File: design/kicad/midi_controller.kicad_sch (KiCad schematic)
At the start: 4 parts, among them U1 CD74HC4067M

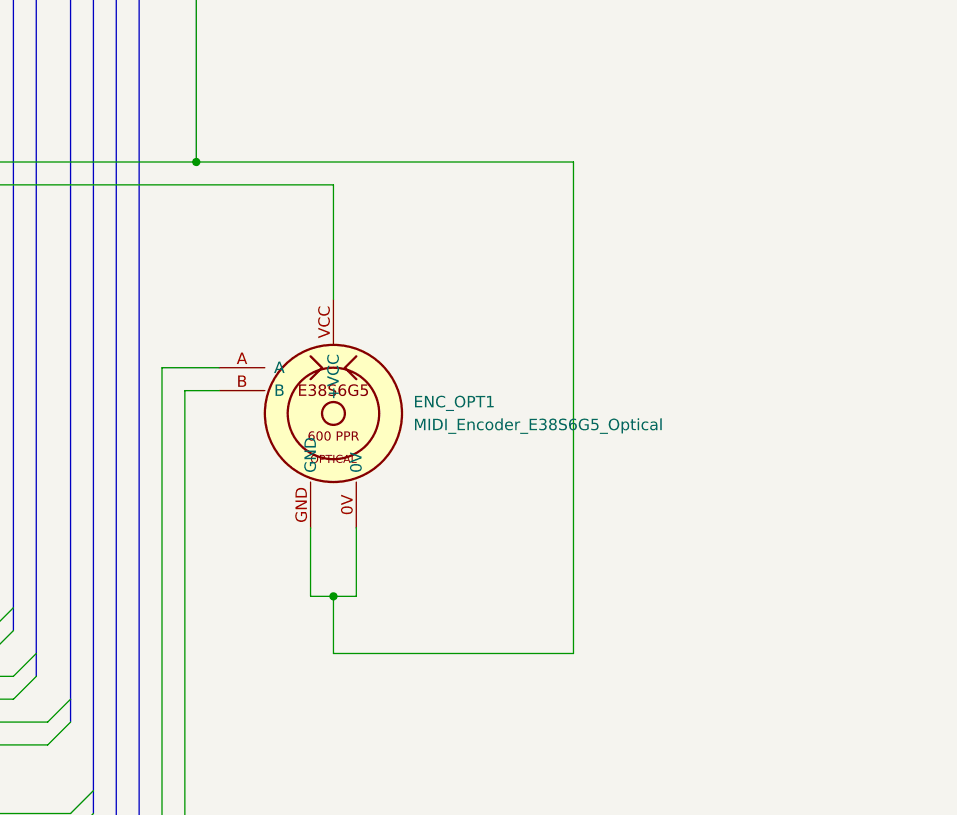
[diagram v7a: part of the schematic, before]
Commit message: Update kicad binary files
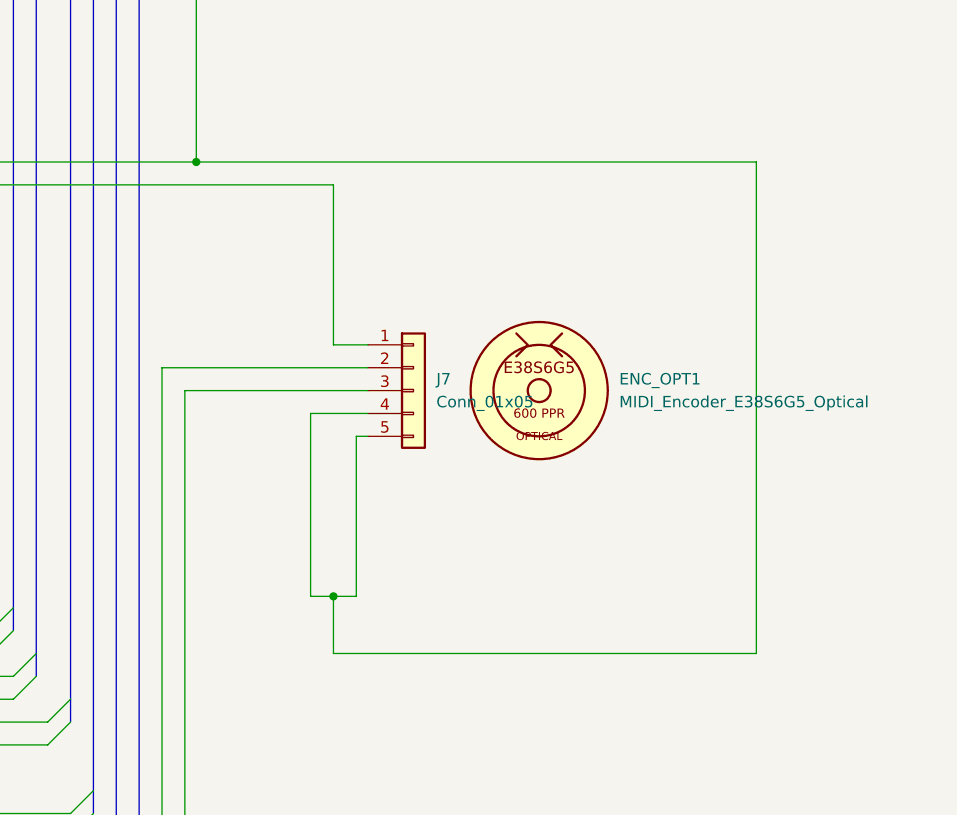
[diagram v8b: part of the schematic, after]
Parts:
- added J7: Conn_01x05, Connector_JST:JST_XH_B5B-XH-A_1x05_P2.50mm_Vertical, symbol Connector_Generic:Conn_01x05
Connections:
- net Buttons_Momentary/GND: now also J7.4 (GND), J7.5 (0V); no longer ENC_OPT1.0V, ENC_OPT1.GND
- net at MCU1.25 (33_MCLK2): now also J7.3 (B); no longer ENC_OPT1.B
- net at MCU1.26 (34_RX8): now also J7.2 (A); no longer ENC_OPT1.A
- net at MCU1.48 (VIN): now also J7.1 (VCC); no longer ENC_OPT1.VCC (+VCC)
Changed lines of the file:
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@@
 	(wire
 		(pts
-			(xy 314.96 146.05) (xy 314.96 158.75)
+			(xy 314.96 146.05) (xy 314.96 163.83)
 		)
 		(stroke
@@
 	(wire
 		(pts
-			(xy 298.45 168.91) (xy 302.26 168.91)
+			(xy 298.45 168.91) (xy 318.77 168.91)
 		)
 		(stroke
@@
 	(wire
 		(pts
+			(xy 312.42 171.45) (xy 312.42 191.77)
+		)
+		(stroke
+			(width 0)
+			(type default)
+		)
+	)
+	(wire
+		(pts
 			(xy 214.63 220.98) (xy 288.29 220.98)
 		)
@@
 	(wire
 		(pts
-			(xy 312.42 184.15) (xy 312.42 191.77)
-		)
-		(stroke
-			(width 0)
-			(type default)
-		)
-	)
-	(wire
-		(pts
 			(xy 125.73 198.12) (xy 158.75 198.12)
 		)
@@
 	(wire
 		(pts
-			(xy 341.63 143.51) (xy 299.72 143.51)
+			(xy 361.95 143.51) (xy 299.72 143.51)
 		)
 		(stroke
@@
 	(wire
 		(pts
+			(xy 312.42 171.45) (xy 318.77 171.45)
+		)
+		(stroke
+			(width 0)
+			(type default)
+		)
+	)
+	(wire
+		(pts
 			(xy 215.9 60.96) (xy 72.39 60.96)
 		)
@@
 	(wire
 		(pts
-			(xy 302.26 166.37) (xy 295.91 166.37)
+			(xy 295.91 166.37) (xy 318.77 166.37)
 		)
 		(stroke
@@
 	(wire
 		(pts
-			(xy 341.63 198.12) (xy 341.63 143.51)
+			(xy 361.95 198.12) (xy 361.95 143.51)
 		)
 		(stroke
@@
 	(wire
 		(pts
+			(xy 317.5 173.99) (xy 318.77 173.99)
+		)
+		(stroke
+			(width 0)
+			(type default)
+		)
+	)
+	(wire
+		(pts
 			(xy 160.02 107.95) (xy 160.02 125.73)
 		)
@@
 	(wire
 		(pts
+			(xy 314.96 163.83) (xy 318.77 163.83)
+		)
+		(stroke
+			(width 0)
+			(type default)
+		)
+	)
+	(wire
+		(pts
 			(xy 153.67 152.4) (xy 233.68 152.4)
 		)
@@
 	(wire
 		(pts
-			(xy 314.96 198.12) (xy 341.63 198.12)
+			(xy 314.96 198.12) (xy 361.95 198.12)
 		)
 		(stroke
@@
 	(wire
 		(pts
-			(xy 317.5 184.15) (xy 317.5 191.77)
-		)
-		(stroke
-			(width 0)
-			(type default)
-		)
-	)
-	(wire
-		(pts
 			(xy 138.43 182.88) (xy 158.75 182.88)
 		)
@@
 		(pts
 			(xy 314.96 191.77) (xy 317.5 191.77)
+		)
+		(stroke
+			(width 0)
+			(type default)
+		)
+	)
+	(wire
+		(pts
+			(xy 317.5 173.99) (xy 317.5 191.77)
 		)
 		(stroke
@@
 	(symbol
 		(lib_id "midi_controller:MIDI_Encoder_E38S6G5_Optical")
-		(at 314.96 171.45 0)
+		(at 337.82 168.91 0)
+		(unit 1)
+		(exclude_from_sim no)
+		(in_bom yes)
+		(on_board no)
+		(dnp no)
+		(fields_autoplaced yes)
+		(property "Reference" "ENC_OPT1"
+			(at 346.71 167.6399 0)
+			(effects
+				(font
+					(size 1.27 1.27)
+				)
+				(justify left)
+			)
+		)
+		(property "Value" "MIDI_Encoder_E38S6G5_Optical"
+			(at 346.71 170.1799 0)
+			(effects
+				(font
+					(size 1.27 1.27)
+				)
+				(justify left)
+			)
+		)
+		(property "Footprint" "midi_controller:E38S6G5_Optical_Encoder"
+			(at 337.82 179.07 0)
+			(effects
+				(font
+					(size 1.27 1.27)
+				)
+				(hide yes)
+			)
+		)
+		(property "Datasheet" ""
+			(at 337.82 181.61 0)
+			(effects
+				(font
+					(size 1.27 1.27)
+				)
+				(hide yes)
+			)
+		)
+		(property "Description" "E38S6G5 Series Optical Rotary Encoder, 600 pulses/revolution, Open Collector NPN output"
+			(at 337.82 168.91 0)
+			(effects
+				(font
+					(size 1.27 1.27)
+				)
+				(hide yes)
+			)
+		)
+		(instances
+			(project ""
+				(path "/9e44e663-00d0-4f33-bf1f-c4ad78deb554"
+					(reference "ENC_OPT1")
+					(unit 1)
+				)
+			)
+		)
+	)
+	(symbol
+		(lib_id "Connector_Generic:Conn_01x05")
+		(at 323.85 168.91 0)
 		(unit 1)
 		(exclude_from_sim no)
@@
 		(dnp no)
 		(fields_autoplaced yes)
-		(property "Reference" "ENC_OPT1"
-			(at 323.85 170.1799 0)
+		(property "Reference" "J7"
+			(at 326.39 167.6399 0)
 			(effects
 				(font
@@
 			)
 		)
-		(property "Value" "MIDI_Encoder_E38S6G5_Optical"
-			(at 323.85 172.7199 0)
+		(property "Value" "Conn_01x05"
+			(at 326.39 170.1799 0)
 			(effects
 				(font
@@
 			)
 		)
-		(property "Footprint" "midi_controller:E38S6G5_Optical_Encoder"
-			(at 314.96 181.61 0)
+		(property "Footprint" "Connector_JST:JST_XH_B5B-XH-A_1x05_P2.50mm_Vertical"
+			(at 323.85 168.91 0)
 			(effects
 				(font
@@
 			)
 		)
-		(property "Datasheet" ""
-			(at 314.96 184.15 0)
+		(property "Datasheet" "~"
+			(at 323.85 168.91 0)
 			(effects
 				(font
@@
 			)
 		)
-		(property "Description" "E38S6G5 Series Optical Rotary Encoder, 600 pulses/revolution, Open Collector NPN output"
-			(at 314.96 171.45 0)
+		(property "Description" "Generic connector, single row, 01x05, script generated (kicad-library-utils/schlib/autogen/connector/)"
+			(at 323.85 168.91 0)
 			(effects
 				(font
@@
 			)
 		)
-		(pin "B"
-		)
-		(pin "0V"
-		)
-		(pin "VCC"
-		)
-		(pin "GND"
-		)
-		(pin "A"
+		(pin "5"
+		)
+		(pin "2"
+		)
+		(pin "1"
+		)
+		(pin "3"
+		)
+		(pin "4"
 		)
 		(instances
 			(project ""
 				(path "/9e44e663-00d0-4f33-bf1f-c4ad78deb554"
-					(reference "ENC_OPT1")
+					(reference "J7")
 					(unit 1)
 				)
